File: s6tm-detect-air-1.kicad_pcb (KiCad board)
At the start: 2 copper layers, 67 x 67 mm, 82 parts, among them J1 Conn_01x04, J2 TC2030, J3 Conn_01x04, J4 Conn_01x04, J5 Conn_01x04_Pin, J6 Conn_01x08, SW1 SW_Push, SW2 SW_Push, U1 SYS1002-H2, U10 004-1-0100, U2 MiCS-5524, U3 LMC6482, U4 HT753-1, U5 SN65HVD230, U6 STM32F103C8Tx, U7 HTU21, U8 LM73100, U9 ENS16x, Y1 8M

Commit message: pcb: add uart routing
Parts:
- moved D7 3.78 mm to (145.5, 115.5)
- moved R10 3.78 mm to (144.0, 115.5)
- moved C5 3.76 mm to (142.0, 115.5)
- moved J5 1.25 mm to (138.5, 115.5)
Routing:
- net /S88_TX: track 0.00 -> 36.9 mm, vias 0 -> 1
- net /S88_RX: track 0.00 -> 36.1 mm, vias 0 -> 1
- net /U0TXD: track 0.00 -> 7.06 mm
- net /U0RXD: track 0.00 -> 5.55 mm
- net /SWDIO: track 7.23 -> 6.65 mm
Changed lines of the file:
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@@
 	(footprint "Resistor_SMD:R_0402_1005Metric"
 		(layer "F.Cu")
-		(at 144.5 111.75 -90)
+		(at 144 115.5 -90)
 		(descr "Resistor SMD 0402 (1005 Metric), square (rectangular) end terminal, IPC-7351 nominal, (Body size source: IPC-SM-782 page 72, https://www.pcb-3d.com/wordpress/wp-content/uploads/ipc-sm-782a_amendment_1_and_2.pdf)")
 		(tags "resistor")
@@
 	(footprint "Capacitor_SMD:C_0805_2012Metric"
 		(layer "F.Cu")
-		(at 142.25 111.75 -90)
+		(at 142 115.5 -90)
 		(descr "Capacitor SMD 0805 (2012 Metric), square (rectangular) end terminal, IPC-7351 nominal, (Body size source: IPC-SM-782 page 76, https://www.pcb-3d.com/wordpress/wp-content/uploads/ipc-sm-782a_amendment_1_and_2.pdf, https://docs.google.com/spreadsheets/d/1BsfQQcO9C6DZCsRaXUlFlo91Tg2WpOkGARC1WS5S8t0/edit?usp=sharing)")
 		(tags "capacitor")
@@
 	(footprint "LED_SMD:LED_0805_2012Metric"
 		(layer "F.Cu")
-		(at 146 111.75 -90)
+		(at 145.5 115.5 -90)
 		(descr "LED SMD 0805 (2012 Metric), square (rectangular) end terminal, IPC-7351 nominal, (Body size source: https://docs.google.com/spreadsheets/d/1BsfQQcO9C6DZCsRaXUlFlo91Tg2WpOkGARC1WS5S8t0/edit?usp=sharing)")
 		(tags "LED")
@@
 	(footprint "Connector_PinHeader_2.54mm:PinHeader_1x04_P2.54mm_Vertical"
 		(layer "F.Cu")
-		(at 139.75 115.5 -90)
+		(at 138.5 115.5 -90)
 		(descr "Through hole straight pin header, 1x04, 2.54mm pitch, single row")
 		(tags "Through hole pin header THT 1x04 2.54mm single row")
@@
 	)
 	(via
-		(at 145 114)
+		(at 146.75 114.5)
 		(size 0.9)
 		(drill 0.4)
@@
 	)
 	(via
-		(at 144 106.25)
+		(at 145.467071 106.425552)
 		(size 0.7)
 		(drill 0.3)
@@
 	)
 	(via
-		(at 142.25 114)
+		(at 142 117.75)
 		(size 0.9)
 		(drill 0.4)
@@
 	)
 	(segment
-		(start 143.25 105.75)
-		(end 142.25 104.75)
+		(start 132.8375 113.5425)
+		(end 132.8375 109.25)
 		(width 0.3)
 		(layer "F.Cu")
-		(net "/SWDIO")
+		(net "/U0TXD")
 	)
 	(segment
-		(start 143.825 107.325)
-		(end 143.25 106.75)
+		(start 130.88 115.5)
+		(end 132.8375 113.5425)
 		(width 0.3)
 		(layer "F.Cu")
-		(net "/SWDIO")
+		(net "/U0TXD")
 	)
 	(segment
-		(start 142.25 104.75)
-		(end 141.1625 104.75)
+		(start 134.25 111.75)
+		(end 134.25 110.6625)
 		(width 0.3)
 		(layer "F.Cu")
-		(net "/SWDIO")
+		(net "/U0RXD")
 	)
 	(segment
-		(start 143.25 106.75)
-		(end 143.25 105.75)
+		(start 135.96 115.5)
+		(end 135.96 113.46)
 		(width 0.3)
 		(layer "F.Cu")
-		(net "/SWDIO")
+		(net "/U0RXD")
+	)
+	(segment
+		(start 135.96 113.46)
+		(end 134.25 111.75)
+		(width 0.3)
+		(layer "F.Cu")
+		(net "/U0RXD")
+	)
+	(segment
+		(start 150.5 110.5)
+		(end 151.75 109.25)
+		(width 0.3)
+		(layer "F.Cu")
+		(net "/S88_TX")
+	)
+	(segment
+		(start 141.1625 106.75)
+		(end 142.25 106.75)
+		(width 0.3)
+		(layer "F.Cu")
+		(net "/S88_TX")
+	)
+	(segment
+		(start 142.25 106.75)
+		(end 143.5 108)
+		(width 0.3)
+		(layer "F.Cu")
+		(net "/S88_TX")
+	)
+	(segment
+		(start 144.5 110.5)
+		(end 150.5 110.5)
+		(width 0.3)
+		(layer "F.Cu")
+		(net "/S88_TX")
+	)
+	(segment
+		(start 143.5 108)
+		(end 143.5 109.5)
+		(width 0.3)
+		(layer "F.Cu")
+		(net "/S88_TX")
+	)
+	(segment
+		(start 151.75 109.25)
+		(end 151.75 102.75)
+		(width 0.3)
+		(layer "F.Cu")
+		(net "/S88_TX")
+	)
+	(segment
+		(start 143.5 109.5)
+		(end 144.5 110.5)
+		(width 0.3)
+		(layer "F.Cu")
+		(net "/S88_TX")
+	)
+	(via
+		(at 151.75 102.75)
+		(size 0.7)
+		(drill 0.3)
+		(layers "F.Cu" "B.Cu")
+		(net "/S88_TX")
+	)
+	(segment
+		(start 151.75 102.75)
+		(end 150.75 102.75)
+		(width 0.3)
+		(layer "B.Cu")
+		(net "/S88_TX")
+	)
+	(segment
+		(start 150.75 102.75)
+		(end 148 100)
+		(width 0.3)
+		(layer "B.Cu")
+		(net "/S88_TX")
+	)
+	(segment
+		(start 148 89.98)
+		(end 149.4 88.58)
+		(width 0.3)
+		(layer "B.Cu")
+		(net "/S88_TX")
+	)
+	(segment
+		(start 148 100)
+		(end 148 89.98)
+		(width 0.3)
+		(layer "B.Cu")
+		(net "/S88_TX")
+	)
+	(segment
+		(start 144.5 109.75)
+		(end 150.25 109.75)
+		(width 0.3)
+		(layer "F.Cu")
+		(net "/S88_RX")
+	)
+	(segment
+		(start 150.25 109.75)
+		(end 151 109)
+		(width 0.3)
+		(layer "F.Cu")
+		(net "/S88_RX")
+	)
+	(segment
+		(start 144 109.25)
+		(end 144.5 109.75)
+		(width 0.3)
+		(layer "F.Cu")
+		(net "/S88_RX")
+	)
+	(segment
+		(start 144 107.75)
+		(end 144 109.25)
+		(width 0.3)
+		(layer "F.Cu")
+		(net "/S88_RX")
+	)
+	(segment
+		(start 142.5 106.25)
+		(end 144 107.75)
+		(width 0.3)
+		(layer "F.Cu")
+		(net "/S88_RX")
+	)
+	(segment
+		(start 141.1625 106.25)
+		(end 142.5 106.25)
+		(width 0.3)
+		(layer "F.Cu")
+		(net "/S88_RX")
+	)
+	(segment
+		(start 151 109)
+		(end 151 101.5)
+		(width 0.3)
+		(layer "F.Cu")
+		(net "/S88_RX")
+	)
+	(via
+		(at 151 101.5)
+		(size 0.7)
+		(drill 0.3)
+		(layers "F.Cu" "B.Cu")
+		(net "/S88_RX")
+	)
+	(segment
+		(start 151 87.64)
+		(end 149.4 86.04)
+		(width 0.3)
+		(layer "B.Cu")
+		(net "/S88_RX")
+	)
+	(segment
+		(start 151 101.5)
+		(end 151 87.64)
+		(width 0.3)
+		(layer "B.Cu")
+		(net "/S88_RX")
 	)
 	(segment
@@
 	)
 	(segment
-		(start 144.75 107.325)
-		(end 143.825 107.325)
+		(start 144.575 107.325)
+		(end 142 104.75)
 		(width 0.3)
 		(layer "F.Cu")
@@
 		(width 0.3)
 		(layer "F.Cu")
+		(net "/SWDIO")
+	)
+	(segment
+		(start 144.75 107.325)
+		(end 144.575 107.325)
+		(width 0.3)
+		(layer "F.Cu")
+		(net "/SWDIO")
+	)
+	(segment
+		(start 142 104.75)
+		(end 141.1625 104.75)
+		(width 0.3)
+		(layer "F.Cu")

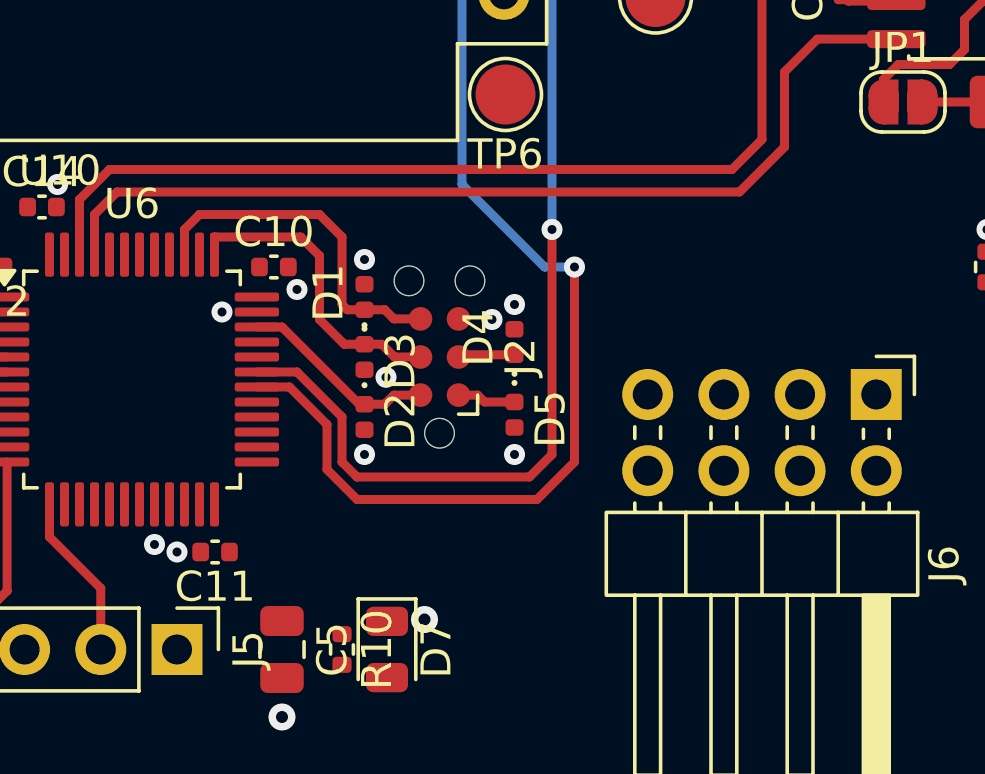
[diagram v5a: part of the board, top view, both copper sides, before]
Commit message: pcb: add gpios routing
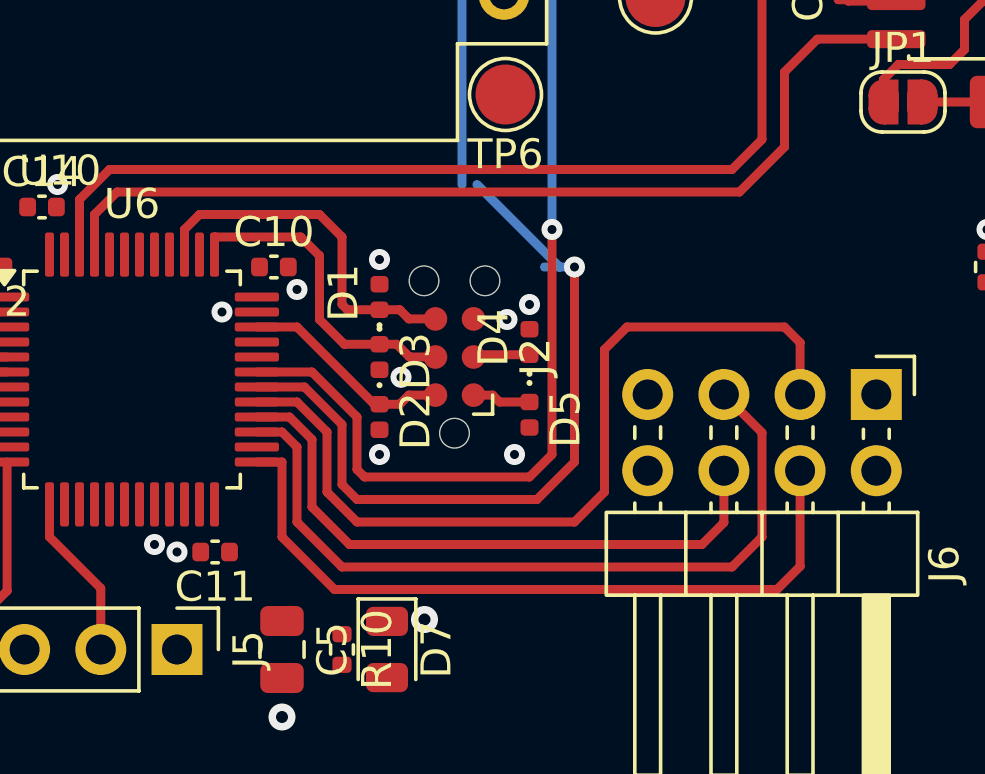
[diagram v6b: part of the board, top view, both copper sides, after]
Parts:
- moved D1 0.50 mm to (145.2, 103.8)
- moved D2 0.50 mm to (145.2, 107.8)
- moved D3 0.50 mm to (145.2, 105.8)
- moved D4 0.50 mm to (150.2, 105.2)
- moved D5 0.50 mm to (150.2, 107.7)
- moved J2 0.50 mm to (147.8, 105.8)
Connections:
- R10 pad 1: Net-(U6-PB12) -> Net-(U6-PB13)
- U6 pad 25: Net-(U6-PB12) -> /PB13
- U6 pad 26: /PB13 -> Net-(U6-PB13)
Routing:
- net /PA8: track 0.00 -> 28.4 mm
- net /PB14: track 0.00 -> 25.9 mm
- net /PB13: track 0.00 -> 24.8 mm
- net /PB15: track 0.00 -> 20.7 mm
- net /SWO: track 11.7 -> 12.2 mm
- net /SWDIO: track 6.65 -> 7.15 mm
- net /SWCLK: track 10.4 -> 10.9 mm

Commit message: pcb: add status led routing
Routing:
- net Net-(U6-PB13): track 0.00 -> 8.91 mm
- net Net-(D7-A): track 0.00 -> 1.68 mm
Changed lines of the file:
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@@
+	)
+	(segment
+		(start 144.4275 116.4375)
+		(end 145.5 116.4375)
+		(width 0.3)
+		(layer "F.Cu")
+		(net "Net-(D7-A)")
+	)
+	(segment
+		(start 144 116.01)
+		(end 144.4275 116.4375)
+		(width 0.3)
+		(layer "F.Cu")
+		(net "Net-(D7-A)")
 	)
 	(segment
@@
 		(net "/PB14")
 	)
+	(segment
+		(start 144 114.99)
+		(end 144 114.75)
+		(width 0.3)
+		(layer "F.Cu")
+		(net "Net-(U6-PB13)")
+	)
+	(segment
+		(start 144 114.75)
+		(end 141.25 112)
+		(width 0.3)
+		(layer "F.Cu")
+		(net "Net-(U6-PB13)")
+	)
+	(segment
+		(start 140.25 108.75)
+		(end 141.1625 108.75)
+		(width 0.3)
+		(layer "F.Cu")
+		(net "Net-(U6-PB13)")
+	)
+	(segment
+		(start 141.25 110.678705)
+		(end 140 109.428705)
+		(width 0.3)
+		(layer "F.Cu")
+		(net "Net-(U6-PB13)")
+	)
+	(segment
+		(start 140 109.428705)
+		(end 140 109)
+		(width 0.3)
+		(layer "F.Cu")
+		(net "Net-(U6-PB13)")
+	)
+	(segment
+		(start 141.25 112)
+		(end 141.25 110.678705)
+		(width 0.3)
+		(layer "F.Cu")
+		(net "Net-(U6-PB13)")
+	)
+	(segment
+		(start 140 109)
+		(end 140.25 108.75)
+		(width 0.3)
+		(layer "F.Cu")
+		(net "Net-(U6-PB13)")
+	)
 	(zone

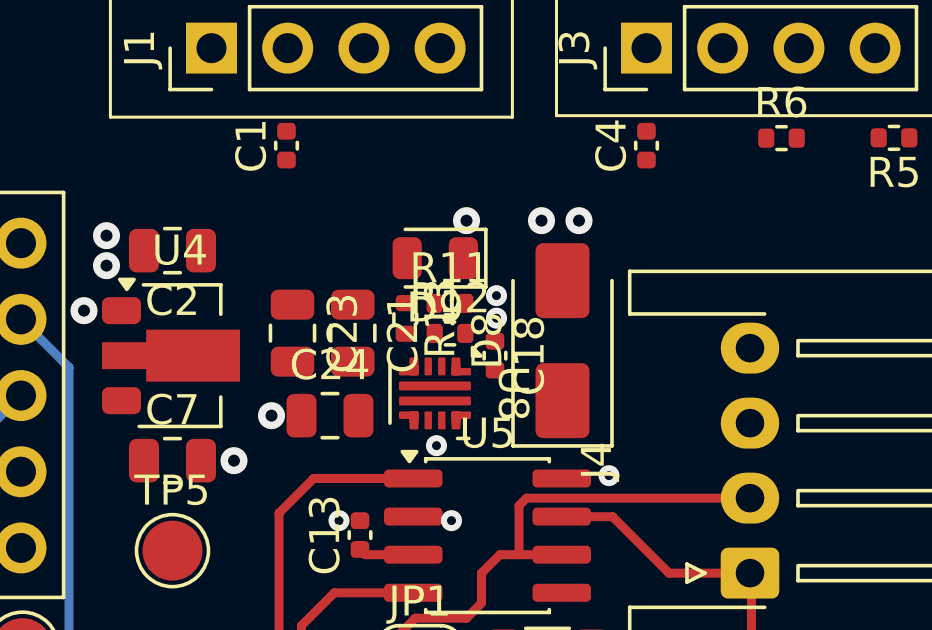
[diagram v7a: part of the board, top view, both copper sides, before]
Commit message: pcb: add efuse routing
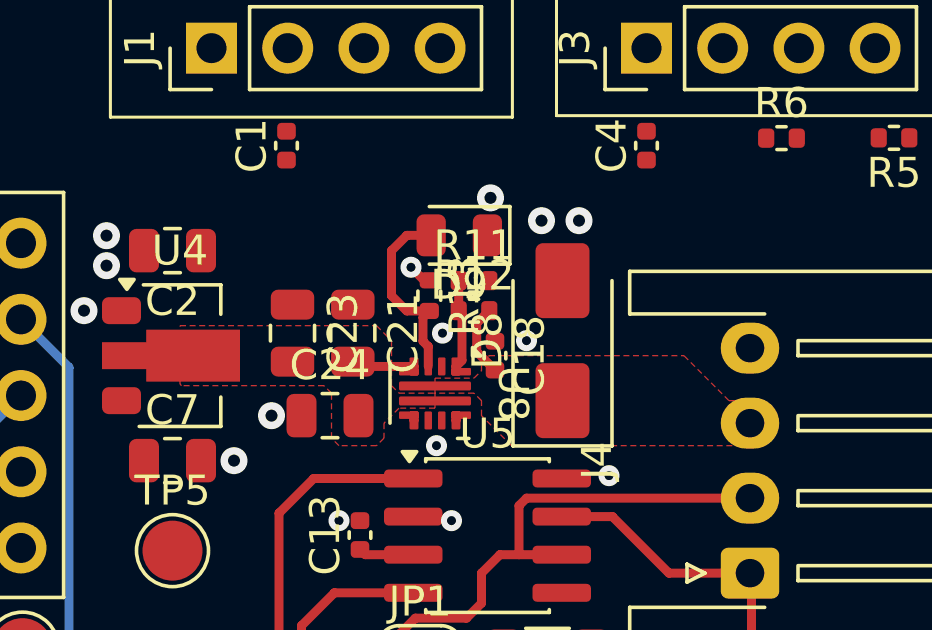
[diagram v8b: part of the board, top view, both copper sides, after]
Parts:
- moved R11 1.10 mm to (164.5, 84.8)
- moved R12 1.10 mm to (164.5, 85.8)
- moved D9 1.10 mm to (164.0, 83.2)
- moved R13 1.10 mm to (163.0, 85.2)
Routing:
- net Net-(D9-A): track 0.00 -> 6.52 mm
- net Net-(U8-EN/UVLO): track 0.00 -> 2.99 mm
- net +VCC: track 0.00 -> 2.41 mm
- net +5V: track 0.00 -> 2.11 mm
- net +3V3: track 3.81 -> 4.60 mm, vias 0 -> 1
- added copper zone on F.Cu, net +5V
- added copper zone on F.Cu, net +VCC
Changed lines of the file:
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@@
 	(footprint "Resistor_SMD:R_0402_1005Metric"
 		(layer "F.Cu")
-		(at 163.7 85.51)
+		(at 164.5 84.75)
 		(descr "Resistor SMD 0402 (1005 Metric), square (rectangular) end terminal, IPC-7351 nominal, (Body size source: IPC-SM-782 page 72, https://www.pcb-3d.com/wordpress/wp-content/uploads/ipc-sm-782a_amendment_1_and_2.pdf)")
 		(tags "resistor")
@@
 	(footprint "Resistor_SMD:R_0402_1005Metric"
 		(layer "F.Cu")
-		(at 162.21 86.01 -90)
+		(at 163.01 85.25 -90)
 		(descr "Resistor SMD 0402 (1005 Metric), square (rectangular) end terminal, IPC-7351 nominal, (Body size source: IPC-SM-782 page 72, https://www.pcb-3d.com/wordpress/wp-content/uploads/ipc-sm-782a_amendment_1_and_2.pdf)")
 		(tags "resistor")
@@
 	(footprint "LED_SMD:LED_0805_2012Metric"
 		(layer "F.Cu")
-		(at 163.21 84 180)
+		(at 164.01 83.24 180)
 		(descr "LED SMD 0805 (2012 Metric), square (rectangular) end terminal, IPC-7351 nominal, (Body size source: https://docs.google.com/spreadsheets/d/1BsfQQcO9C6DZCsRaXUlFlo91Tg2WpOkGARC1WS5S8t0/edit?usp=sharing)")
 		(tags "LED")
@@
 	(footprint "Resistor_SMD:R_0402_1005Metric"
 		(layer "F.Cu")
-		(at 163.7 86.51)
+		(at 164.5 85.75)
 		(descr "Resistor SMD 0402 (1005 Metric), square (rectangular) end terminal, IPC-7351 nominal, (Body size source: IPC-SM-782 page 72, https://www.pcb-3d.com/wordpress/wp-content/uploads/ipc-sm-782a_amendment_1_and_2.pdf)")
 		(tags "resistor")
@@
 	)
 	(via
-		(at 165.25 86)
-		(size 0.7)
-		(drill 0.3)
-		(layers "F.Cu" "B.Cu")
-		(free yes)
-		(net "GND")
-	)
-	(via
 		(at 142.5 103.5)
 		(size 0.7)
@@
 	)
 	(via
-		(at 165.25 85.25)
+		(at 166.25 86.75)
+		(size 0.7)
+		(drill 0.3)
+		(layers "F.Cu" "B.Cu")
+		(free yes)
+		(net "GND")
+	)
+	(via
+		(at 163.449192 86.5)
 		(size 0.7)
 		(drill 0.3)
@@
 	)
 	(via
-		(at 164.25 82.75)
+		(at 165.05 81.99)
 		(size 0.9)
 		(drill 0.4)
@@
 	)
 	(segment
+		(start 165.2 87.73)
+		(end 164.59 87.12)
+		(width 0.3)
+		(layer "F.Cu")
+		(net "+VCC")
+	)
+	(segment
+		(start 164.59 87.12)
+		(end 164.59 86.17)
+		(width 0.3)
+		(layer "F.Cu")
+		(net "+VCC")
+	)
+	(segment
+		(start 164.59 86.17)
+		(end 165.01 85.75)
+		(width 0.3)
+		(layer "F.Cu")
+		(net "+VCC")
+	)
+	(segment
 		(start 173.75 96.5)
 		(end 173 97.25)
@@
 	)
 	(segment
+		(start 162.5 87.61)
+		(end 160.62 87.61)
+		(width 0.3)
+		(layer "F.Cu")
+		(net "+5V")
+	)
+	(segment
+		(start 160.62 87.61)
+		(end 160.46 87.45)
+		(width 0.3)
+		(layer "F.Cu")
+		(net "+5V")
+	)
+	(segment
 		(start 150.25 107.25)
 		(end 149.25 107.25)
@@
 	)
 	(segment
+		(start 162.83573 84.74)
+		(end 162.399999 84.304269)
+		(width 0.3)
+		(layer "F.Cu")
+		(net "+3V3")
+	)
+	(segment
 		(start 149.25 107.25)
 		(end 149.02 107.02)
@@
 	)
 	(segment
+		(start 163.01 84.74)
+		(end 162.83573 84.74)
+		(width 0.3)
+		(layer "F.Cu")
+		(net "+3V3")
+	)
+	(segment
 		(start 160.875 93.885)
 		(end 160.7 93.71)
@@
 		(net "+3V3")
 	)
+	(via
+		(at 162.399999 84.304269)
+		(size 0.7)
+		(drill 0.3)
+		(layers "F.Cu" "B.Cu")
+		(net "+3V3")
+	)
 	(segment
 		(start 144.4275 116.4375)
@@
 	)
 	(segment
+		(start 164.099192 85.859192)
+		(end 163.99 85.75)
+		(width 0.3)
+		(layer "F.Cu")
+		(net "Net-(U8-EN{slash}UVLO)")
+	)
+	(segment
+		(start 164.099192 87.410808)
+		(end 164.099192 85.859192)
+		(width 0.3)
+		(layer "F.Cu")
+		(net "Net-(U8-EN{slash}UVLO)")
+	)
+	(segment
+		(start 163.9 87.61)
+		(end 164.099192 87.410808)
+		(width 0.3)
+		(layer "F.Cu")
+		(net "Net-(U8-EN{slash}UVLO)")
+	)
+	(segment
+		(start 163.99 85.75)
+		(end 163.99 84.75)
+		(width 0.3)
+		(layer "F.Cu")
+		(net "Net-(U8-EN{slash}UVLO)")
+	)
+	(segment
+		(start 162.799192 85.970808)
+		(end 163.01 85.76)
+		(width 0.3)
+		(layer "F.Cu")
+		(net "Net-(D9-A)")
+	)
+	(segment
+		(start 162.975 86.945047)
+		(end 162.799192 86.769239)
+		(width 0.3)
+		(layer "F.Cu")
+		(net "Net-(D9-A)")
+	)
+	(segment
+		(start 161.75 85.25)
+		(end 161.75 83.75)
+		(width 0.3)
+		(layer "F.Cu")
+		(net "Net-(D9-A)")
+	)
+	(segment
+		(start 162.26 83.24)
+		(end 163.0725 83.24)
+		(width 0.3)
+		(layer "F.Cu")
+		(net "Net-(D9-A)")
+	)
+	(segment
+		(start 163.01 85.76)
+		(end 162.26 85.76)
+		(width 0.3)
+		(layer "F.Cu")
+		(net "Net-(D9-A)")
+	)
+	(segment
+		(start 161.75 83.75)
+		(end 162.26 83.24)
+		(width 0.3)
+		(layer "F.Cu")
+		(net "Net-(D9-A)")
+	)
+	(segment
+		(start 162.799192 86.769239)
+		(end 162.799192 85.970808)
+		(width 0.3)
+		(layer "F.Cu")
+		(net "Net-(D9-A)")
+	)
+	(segment
+		(start 162.975 87.61)
+		(end 162.975 86.945047)
+		(width 0.3)
+		(layer "F.Cu")
+		(net "Net-(D9-A)")
+	)
+	(segment
+		(start 162.26 85.76)
+		(end 161.75 85.25)
+		(width 0.3)
+		(layer "F.Cu")
+		(net "Net-(D9-A)")
+	)
+	(segment
 		(start 165.4875 97.25)
 		(end 163.35 97.25)
@@
 	)
 	(zone
+		(net "+5V")
+		(layer "F.Cu")
+		(hatch edge 0.5)
+		(priority 2)
+		(connect_pads yes
+			(clearance 0.2)
+		)
+		(min_thickness 0.15)
+		(fill yes
+			(thermal_gap 0.35)
+			(thermal_bridge_width 0.35)
+			(island_removal_mode 1)
+		)
+		(polygon
+			(pts
+				(xy 163.2 88.51) (xy 163.2 89) (xy 162 89) (xy 161.5 89.5) (xy 161.5 90) (xy 161.25 90.25) (xy 160 90.25)
+				(xy 159.75 90) (xy 159.75 88.5) (xy 159.5 88.25) (xy 154.75 88.25) (xy 154.7 88.2) (xy 154.7 86.25)
+				(xy 161.25 86.25) (xy 161.75 86.75) (xy 161.75 88.25) (xy 162 88.5) (xy 163.19 88.5)
+			)
+		)
+	)
+	(zone
+		(net "+VCC")
+		(layer "F.Cu")
+		(hatch edge 0.5)
+		(priority 1)
+		(connect_pads yes
+			(clearance 0.2)
+		)
+		(min_thickness 0.15)
+		(fill yes
+			(thermal_gap 0.35)
+			(thermal_bridge_width 0.35)
+			(island_removal_mode 1)
+		)
+		(polygon
+			(pts
+				(xy 173.75 90.25) (xy 165.75 90.25) (xy 164.75 89.25) (xy 164.75 88.75) (xy 164.5 88.5) (xy 163.21 88.5)
+				(xy 163.2 88.51) (xy 163.2 88) (xy 164.5 88) (xy 164.75 87.75) (xy 164.75 87.5) (xy 165 87.25) (xy 171.5 87.25)
+				(xy 173 88.75) (xy 173.75 88.75)
+			)
+		)
+	)
+	(zone
